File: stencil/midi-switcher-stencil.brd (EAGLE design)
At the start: 211 x 116.5 mm, 398 parts, among them IC1 6N138, IC10 PIC16F1825SO14, IC11 6N138, IC12 LD1086, IC13 PIC16F1825SO14, IC14 6N138, IC15 LD1086, IC2 PIC16F1825SO14, IC3 LD1086, IC4 PIC16F1825SO14, IC5 6N138, IC6 LD1086, IC7 PIC16F1825SO14, IC8 6N138, IC9 LD1086, Q1 MJD122GDPAK, Q10 MJD122GDPAK, Q11 MJD122GDPAK, Q12 MJD122GDPAK, Q13 MJD122GDPAK, Q14 MJD122GDPAK, Q15 MJD122GDPAK, Q16 MJD122GDPAK, Q17 MJD122GDPAK, Q19 MJD122GDPAK, Q2 MJD122GDPAK, Q20 MJD122GDPAK, Q21 MJD122GDPAK, Q22 MJD122GDPAK, Q23 MJD122GDPAK, Q24 MJD122GDPAK, Q25 MJD122GDPAK, Q26 MJD122GDPAK, Q28 MJD122GDPAK, Q29 MJD122GDPAK, Q3 MJD122GDPAK, Q30 MJD122GDPAK, Q31 MJD122GDPAK, Q32 MJD122GDPAK, Q33 MJD122GDPAK, Q34 MJD122GDPAK, Q35 MJD122GDPAK, Q37 MJD122GDPAK, Q38 MJD122GDPAK, Q39 MJD122GDPAK, Q4 MJD122GDPAK, Q40 MJD122GDPAK, Q41 MJD122GDPAK, Q42 MJD122GDPAK, Q43 MJD122GDPAK, Q44 MJD122GDPAK, Q5 MJD122GDPAK, Q6 MJD122GDPAK, Q7 MJD122GDPAK, Q8 MJD122GDPAK

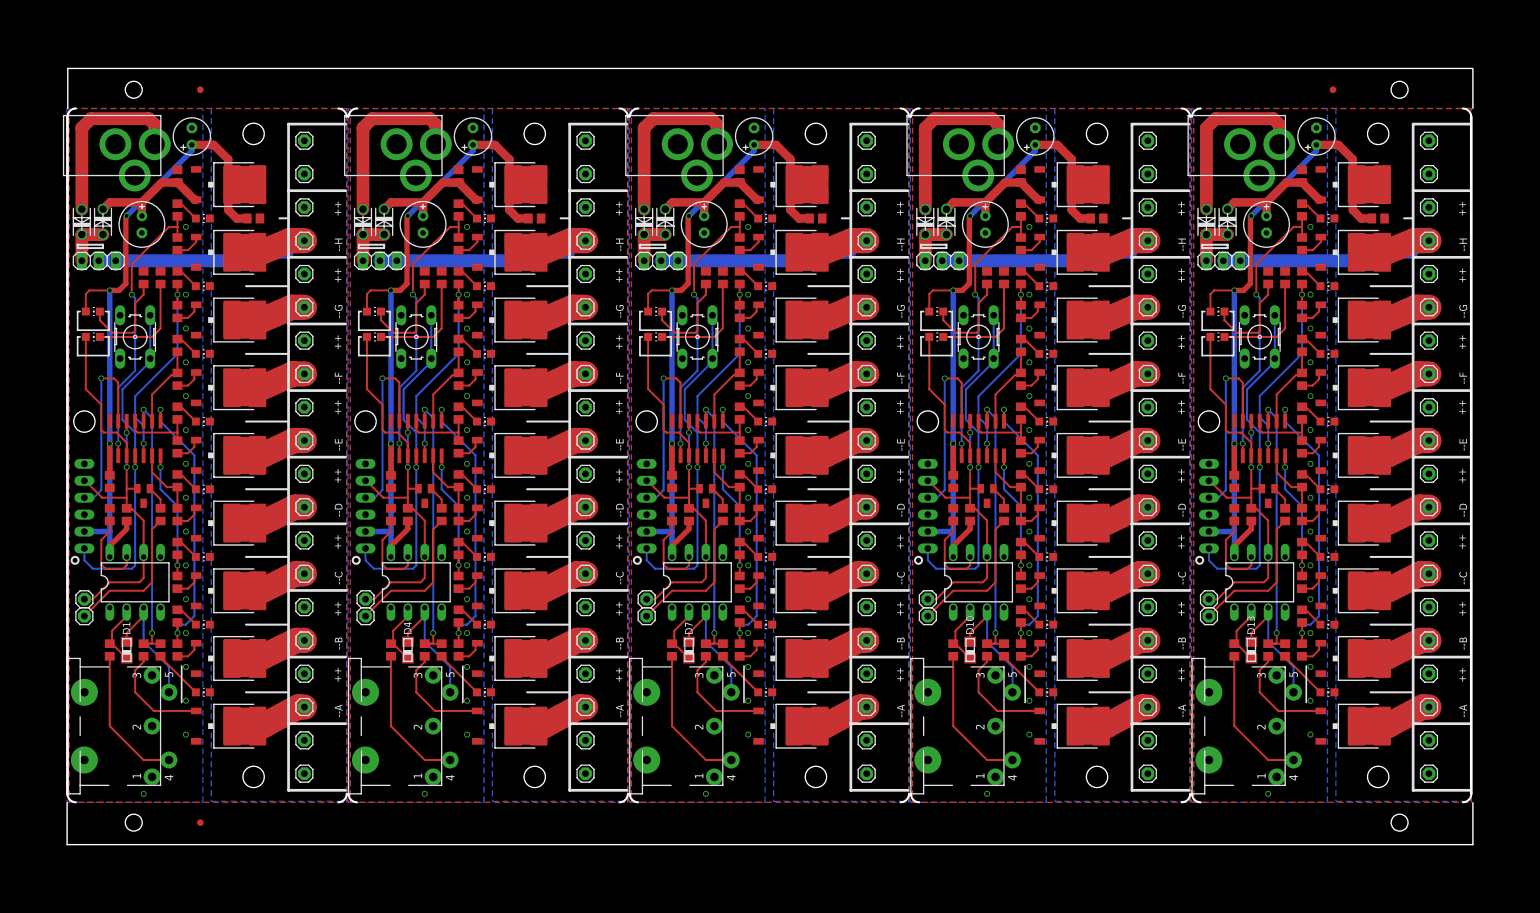
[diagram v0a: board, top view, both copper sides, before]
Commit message: 1.2	24apr20		support relay switcher
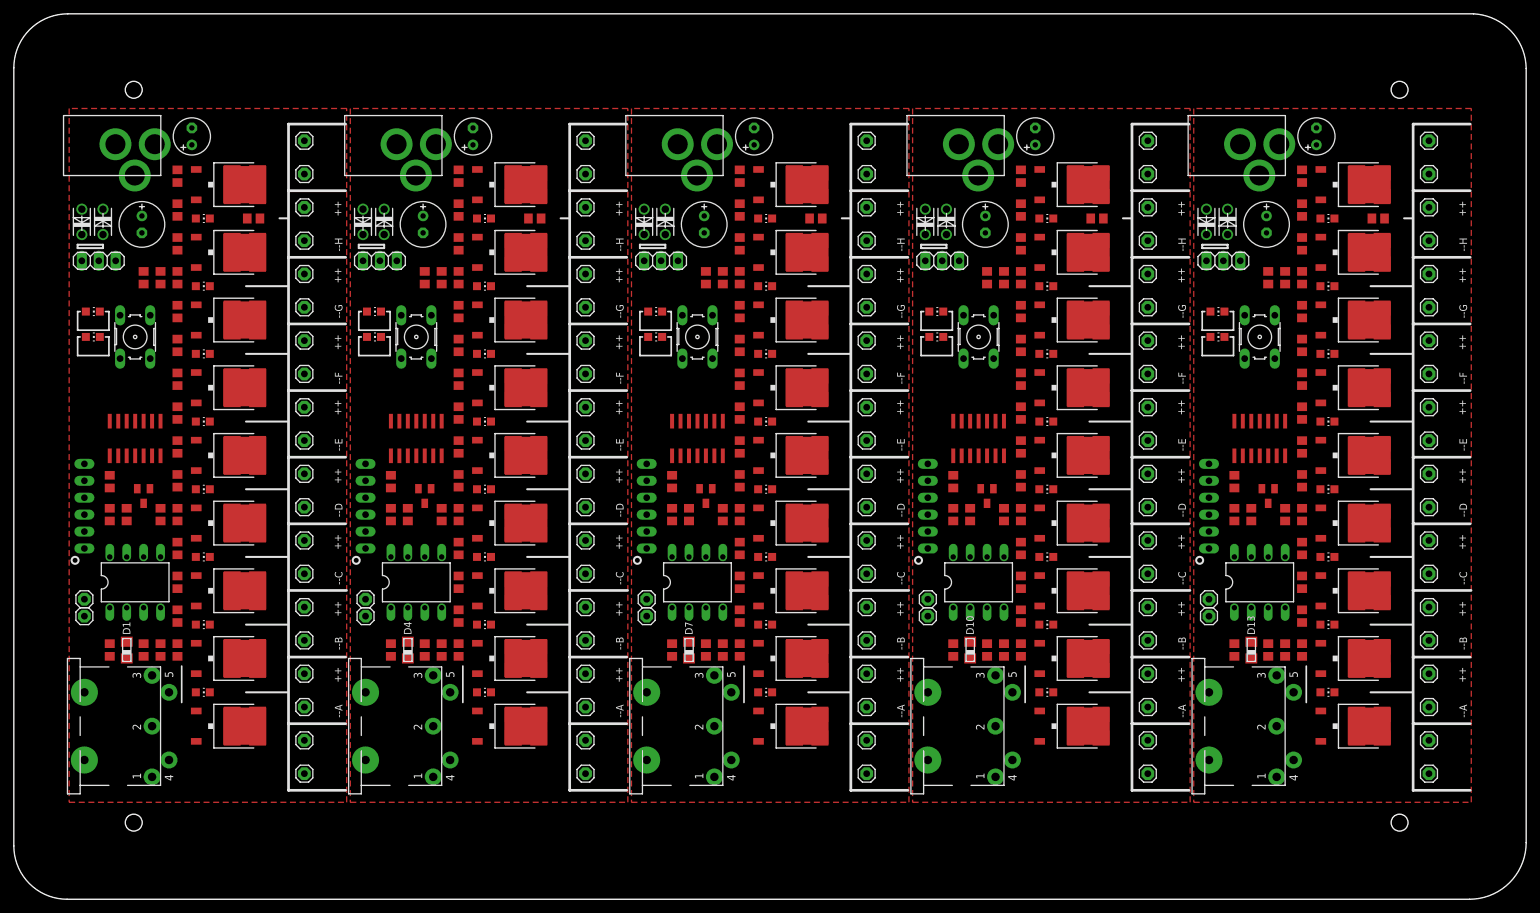
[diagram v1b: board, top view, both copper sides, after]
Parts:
- added E$4: (no value), jason_stencil:STENCILPIN
- E$1, E$2, E$3: device adafruit:FIDUCIAL_1MM -> jason_stencil:STENCILPIN
- moved E$3 180.0 mm to (200.0, -3.00)
- moved E$1 10.0 mm to (10.0, 107.0)
- moved E$2 10.0 mm to (200.0, 107.0)
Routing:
- net +5V4: track 114.9 -> 0.00 mm, vias 3 -> 0
- net +5V3: track 114.9 -> 0.00 mm, vias 3 -> 0
- net +5V2: track 114.9 -> 0.00 mm, vias 3 -> 0
- net +5V: track 114.9 -> 0.00 mm, vias 3 -> 0
- net +5V1: track 114.9 -> 0.00 mm, vias 3 -> 0
- net SWITCH3: track 52.5 -> 0.00 mm, vias 1 -> 0
- net SWITCH1: track 52.5 -> 0.00 mm, vias 1 -> 0
- net SWITCH: track 52.5 -> 0.00 mm, vias 1 -> 0
- net SWITCH2: track 52.5 -> 0.00 mm, vias 1 -> 0
- net SWITCH4: track 52.5 -> 0.00 mm, vias 1 -> 0
- net MIDI_IN3: track 44.2 -> 0.00 mm, vias 2 -> 0
- net MIDI_IN2: track 44.2 -> 0.00 mm, vias 2 -> 0
- net MIDI_IN1: track 44.2 -> 0.00 mm, vias 2 -> 0
- net MIDI_IN: track 44.2 -> 0.00 mm, vias 2 -> 0
- net MIDI_IN4: track 44.2 -> 0.00 mm, vias 2 -> 0
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- removed copper zone on layer 16, net +12V
- removed copper zone on layer 16, net +12V1
- removed copper zone on layer 16, net +12V2
- removed copper zone on layer 16, net +12V3
- removed copper zone on layer 16, net +12V4
- removed copper zone on layer 16, net GND
- removed copper zone on layer 16, net GND1
- removed copper zone on layer 16, net GND2
- removed copper zone on layer 16, net GND3
- removed copper zone on layer 16, net GND4
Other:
- board size 211 x 116.5 mm -> 227 x 132.9 mm
